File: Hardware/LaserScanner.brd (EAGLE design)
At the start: 66 x 77.5 mm, 105 parts, among them J1 USB, J2 !KILL!, J3 KEYSWITCH, J5 ESTOP, J8 Power Input, Q1 MBT3904DW1T1, Q4 2.5A/30V/105mΩ, U1 ESP-WROOM-32, U2 3.3V, U3 CH340C

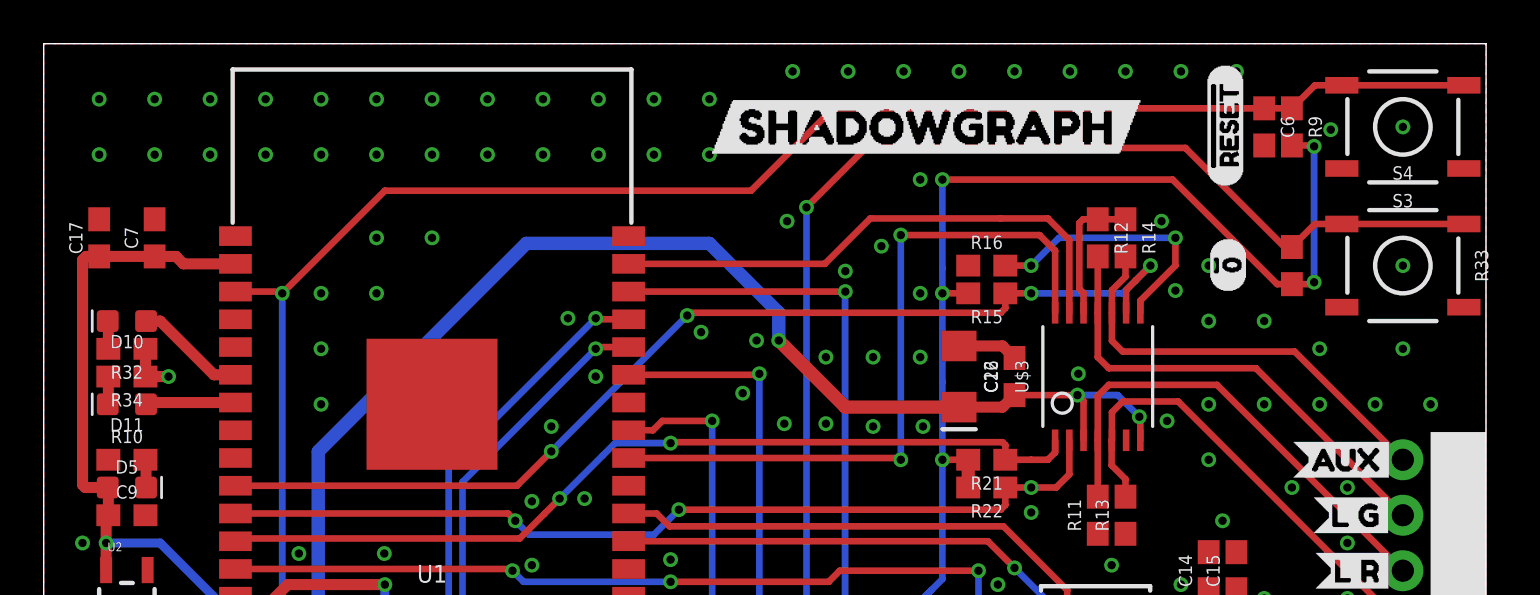
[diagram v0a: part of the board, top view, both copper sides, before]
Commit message: stop using input only pins for led outputs
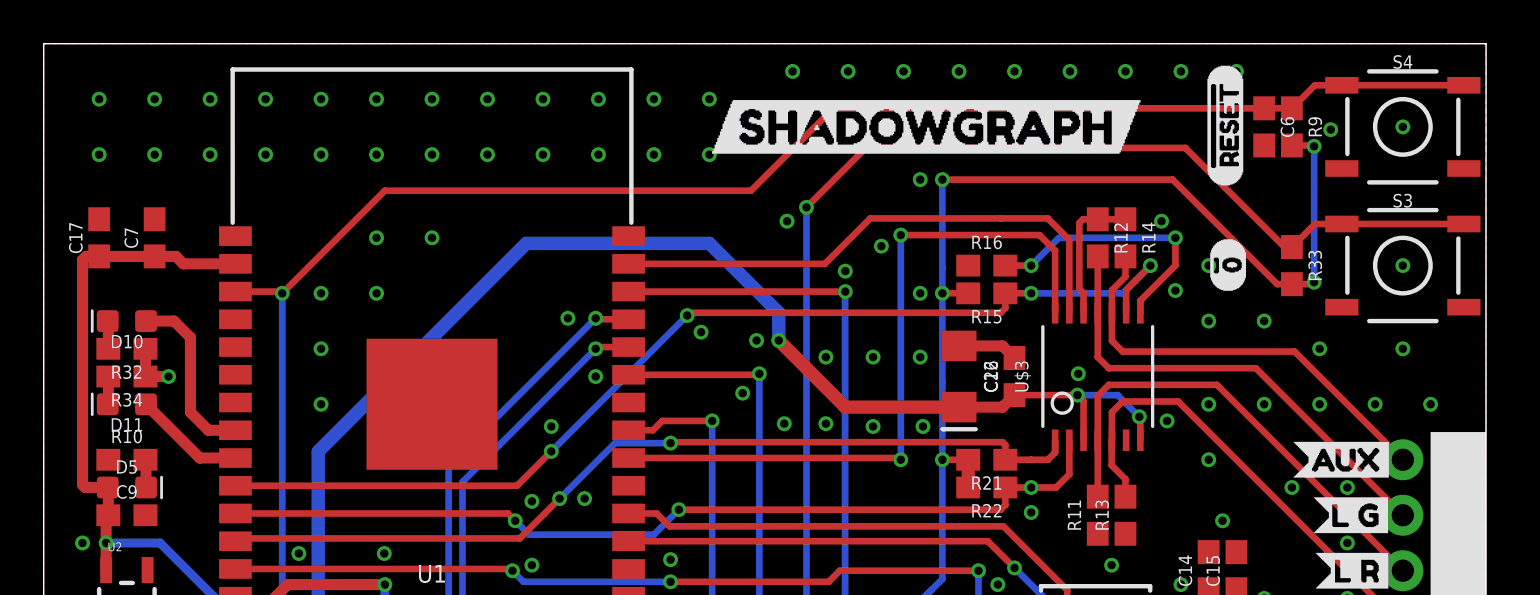
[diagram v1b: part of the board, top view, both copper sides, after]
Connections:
- removed net N$11: U1.29
- removed net N$22: U1.8
- removed net N$23: U1.9
- removed net N$8: U1.26
- net ULED1: now also U1.8; no longer U1.6
- net ULED2: now also U1.9; no longer U1.7
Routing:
- net ULED1: track 5.11 -> 8.17 mm
- net ULED2: track 4.13 -> 5.23 mm
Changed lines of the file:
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@@
 <?xml version="1.0" encoding="utf-8"?>
 <!DOCTYPE eagle SYSTEM "eagle.dtd">
-<eagle version="9.1.3">
+<eagle version="9.2.0">
 <drawing>
 <settings>
-<setting alwaysvectorfont="yes"/>
+<setting alwaysvectorfont="no"/>
 <setting verticaltext="up"/>
 </settings>
@@
 <layer number="18" name="Vias" color="2" fill="1" visible="yes" active="yes"/>
 <layer number="19" name="Unrouted" color="6" fill="1" visible="yes" active="yes"/>
-<layer number="20" name="Dimension" color="15" fill="1" visible="yes" active="yes"/>
+<layer number="20" name="Dimension" color="24" fill="1" visible="yes" active="yes"/>
 <layer number="21" name="tPlace" color="16" fill="1" visible="yes" active="yes"/>
 <layer number="22" name="bPlace" color="14" fill="1" visible="yes" active="yes"/>
@@
 <layer number="44" name="Drills" color="7" fill="1" visible="no" active="yes"/>
 <layer number="45" name="Holes" color="7" fill="1" visible="yes" active="yes"/>
-<layer number="46" name="Milling" color="3" fill="1" visible="yes" active="yes"/>
+<layer number="46" name="Milling" color="3" fill="1" visible="no" active="yes"/>
 <layer number="47" name="Measures" color="7" fill="1" visible="no" active="yes"/>
 <layer number="48" name="Document" color="7" fill="1" visible="no" active="yes"/>
@@
 <layer number="95" name="Names" color="7" fill="1" visible="no" active="no"/>
 <layer number="96" name="Values" color="7" fill="1" visible="no" active="no"/>
-<layer number="2" name="Route2" color="16" fill="1" visible="yes" active="yes"/>
-<layer number="15" name="Route15" color="23" fill="1" visible="yes" active="yes"/>
+<layer number="2" name="Route2" color="16" fill="1" visible="no" active="yes"/>
+<layer number="15" name="Route15" color="23" fill="1" visible="no" active="yes"/>
 <layer number="53" name="tGND_GNDA" color="7" fill="9" visible="no" active="no"/>
 <layer number="54" name="bGND_GNDA" color="1" fill="9" visible="no" active="no"/>
@@
 </element>
 <element name="R33" library="SparkFun-Resistors" package="0603" value="10k" x="57.15" y="67.31" rot="R270">
-<attribute name="NAME" x="65.532" y="67.31" size="0.6096" layer="25" font="vector" ratio="20" rot="R270" align="bottom-center"/>
+<attribute name="NAME" x="57.912" y="67.31" size="0.6096" layer="25" font="vector" ratio="20" rot="R270" align="bottom-center"/>
 <attribute name="PROD_ID" value="RES-00824" x="64.77" y="67.31" size="1.778" layer="27" font="vector" ratio="15" rot="R270" display="off"/>
-<attribute name="VALUE" x="64.008" y="67.31" size="0.6096" layer="27" font="vector" ratio="20" rot="R270" align="top-center"/>
+<attribute name="VALUE" x="56.388" y="67.31" size="0.6096" layer="27" font="vector" ratio="20" rot="R270" align="top-center"/>
 </element>
 <element name="S4" library="SparkFun-Switches" package="TACTILE_SWITCH_SMD_5.2MM" value="USW3" x="62.23" y="73.66">
-<attribute name="NAME" x="62.23" y="71.247" size="0.6096" layer="25" font="vector" ratio="20" align="bottom-center"/>
+<attribute name="NAME" x="62.23" y="76.327" size="0.6096" layer="25" font="vector" ratio="20" align="bottom-center"/>
 <attribute name="PROD_ID" value="SWCH-08247" x="62.23" y="68.58" size="1.778" layer="27" font="vector" ratio="15" display="off"/>
 <attribute name="SF_SKU" value="COM-08720" x="62.23" y="68.58" size="1.778" layer="27" font="vector" ratio="15" display="off"/>
-<attribute name="VALUE" x="62.23" y="65.913" size="0.6096" layer="27" font="vector" ratio="20" align="top-center"/>
+<attribute name="VALUE" x="62.23" y="70.993" size="0.6096" layer="27" font="vector" ratio="20" align="top-center"/>
 </element>
 <element name="D10" library="SparkFun-LED" package="LED-0603" value="BLUE" x="3.81" y="64.77" rot="R180">
+<attribute name="NAME" x="3.81" y="64.135" size="0.6096" layer="25" font="vector" ratio="20" rot="R180" align="bottom-center"/>
 <attribute name="PROD_ID" value="DIO-08575" x="3.81" y="64.77" size="1.778" layer="27" font="vector" ratio="15" rot="R180" display="off"/>
+<attribute name="VALUE" x="3.81" y="65.405" size="0.6096" layer="27" font="vector" ratio="20" rot="R180" align="top-center"/>
 </element>
 <element name="D11" library="SparkFun-LED" package="LED-0603" value="BLUE" x="3.81" y="60.96" rot="R180">
+<attribute name="NAME" x="3.81" y="60.325" size="0.6096" layer="25" font="vector" ratio="20" rot="R180" align="bottom-center"/>
 <attribute name="PROD_ID" value="DIO-08575" x="3.81" y="60.96" size="1.778" layer="27" font="vector" ratio="15" rot="R180" display="off"/>
+<attribute name="VALUE" x="3.81" y="61.595" size="0.6096" layer="27" font="vector" ratio="20" rot="R180" align="top-center"/>
 </element>
 <element name="R32" library="SparkFun-Resistors" package="0603" value="1k" x="3.81" y="63.5" rot="R180">
+<attribute name="NAME" x="3.81" y="62.738" size="0.6096" layer="25" font="vector" ratio="20" rot="R180" align="bottom-center"/>
 <attribute name="PROD_ID" value="RES-07856" x="3.81" y="63.5" size="1.778" layer="27" font="vector" ratio="15" rot="R180" display="off"/>
+<attribute name="VALUE" x="3.81" y="64.262" size="0.6096" layer="27" font="vector" ratio="20" rot="R180" align="top-center"/>
 </element>
 <element name="R34" library="SparkFun-Resistors" package="0603" value="1k" x="3.81" y="62.23" rot="R180">
+<attribute name="NAME" x="3.81" y="61.468" size="0.6096" layer="25" font="vector" ratio="20" rot="R180" align="bottom-center"/>
 <attribute name="PROD_ID" value="RES-07856" x="3.81" y="62.23" size="1.778" layer="27" font="vector" ratio="15" rot="R180" display="off"/>
+<attribute name="VALUE" x="3.81" y="62.992" size="0.6096" layer="27" font="vector" ratio="20" rot="R180" align="top-center"/>
 </element>
 <element name="R35" library="SparkFun-Resistors" package="0603" value="100" x="40.64" y="8.89" rot="R270">
+<attribute name="NAME" x="41.402" y="8.89" size="0.6096" layer="25" font="vector" ratio="20" rot="R270" align="bottom-center"/>
 <attribute name="PROD_ID" value="RES-12438" x="40.64" y="8.89" size="1.778" layer="27" font="vector" ratio="15" rot="R270" display="off"/>
+<attribute name="VALUE" x="39.878" y="8.89" size="0.6096" layer="27" font="vector" ratio="20" rot="R270" align="top-center"/>
 </element>
 <element name="U$7" library="e#stop#jpg" package="E#STOP#JPG" value="" x="57" y="24" rot="R90"/>
@@
 <wire x1="64.77" y1="22.86" x2="64.77" y2="17.78" width="1.2192" layer="16"/>
 </signal>
-<signal name="N$8">
-<contactref element="U1" pad="26"/>
-</signal>
-<signal name="N$11">
-<contactref element="U1" pad="29"/>
-</signal>
-<signal name="N$22">
-<contactref element="U1" pad="8"/>
-</signal>
-<signal name="N$23">
-<contactref element="U1" pad="9"/>
-</signal>
 <signal name="!KILL">
 <contactref element="Q4" pad="1"/>
@@
 <signal name="ULED1">
 <contactref element="D10" pad="A"/>
-<contactref element="U1" pad="6"/>
-<wire x1="4.687" y1="64.77" x2="5.334" y2="64.77" width="0.508" layer="1"/>
-<wire x1="7.794" y1="62.31" x2="8.78" y2="62.31" width="0.508" layer="1"/>
-<wire x1="5.334" y1="64.77" x2="7.794" y2="62.31" width="0.508" layer="1"/>
+<wire x1="4.687" y1="64.77" x2="5.969" y2="64.77" width="0.508" layer="1"/>
+<contactref element="U1" pad="8"/>
+<wire x1="7.54" y1="59.77" x2="8.78" y2="59.77" width="0.508" layer="1"/>
+<wire x1="6.7183" y1="64.0207" x2="5.969" y2="64.77" width="0.508" layer="1"/>
+<wire x1="6.7183" y1="60.5917" x2="7.54" y2="59.77" width="0.508" layer="1"/>
+<wire x1="6.7183" y1="64.0207" x2="6.7183" y2="60.5917" width="0.508" layer="1"/>
 </signal>
 <signal name="ULED2">
 <contactref element="D11" pad="A"/>
-<contactref element="U1" pad="7"/>
-<wire x1="8.78" y1="61.04" x2="4.767" y2="61.04" width="0.508" layer="1"/>
 <wire x1="4.767" y1="61.04" x2="4.687" y2="60.96" width="0.508" layer="1"/>
+<contactref element="U1" pad="9"/>
+<wire x1="4.687" y1="60.96" x2="7.147" y2="58.5" width="0.508" layer="1"/>
+<wire x1="7.147" y1="58.5" x2="8.78" y2="58.5" width="0.508" layer="1"/>
 </signal>
 <signal name="N$38">
